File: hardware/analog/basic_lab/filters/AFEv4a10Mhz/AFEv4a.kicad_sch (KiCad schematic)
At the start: 15 parts, among them J1 Connector_Generic_Conn_01x20, J2 Connector_Generic_Conn_01x02, J3 Connector_Generic_Conn_01x02

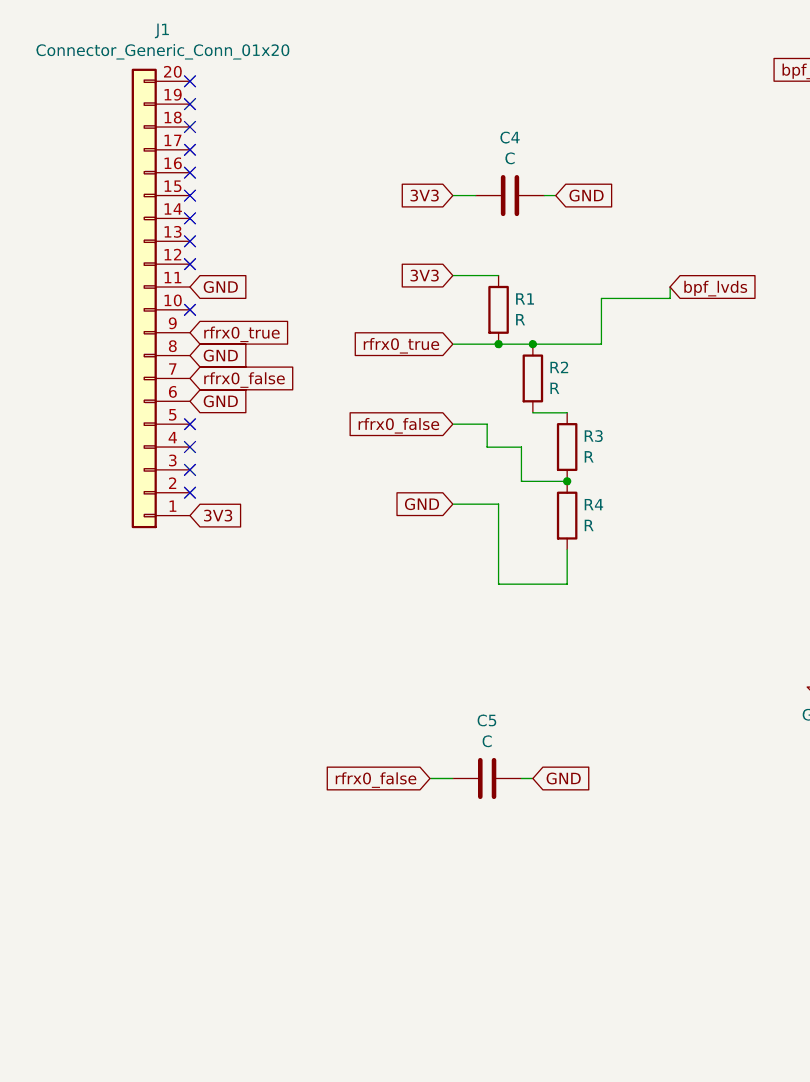
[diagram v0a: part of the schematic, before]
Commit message: started zero DC-offset AFE
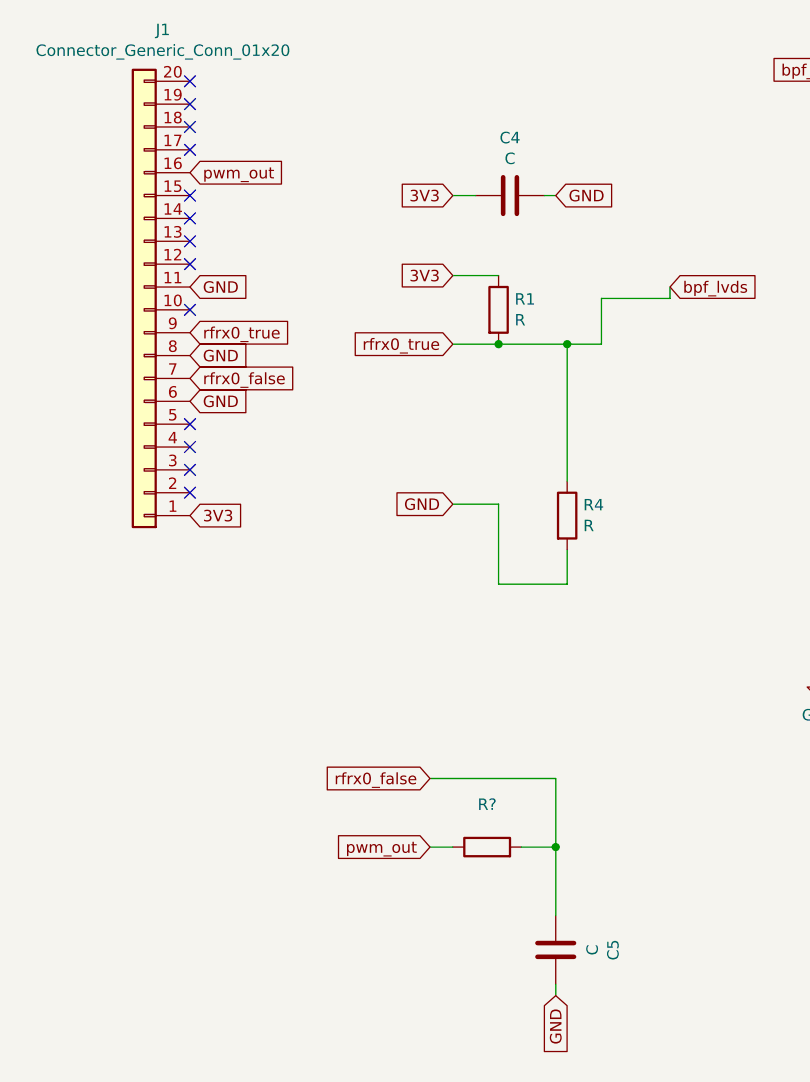
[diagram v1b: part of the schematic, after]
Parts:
- removed R2, R3: R, Resistor_THT:R_Axial_DIN0207_L6.3mm_D2.5mm_P5.08mm_Vertical, symbol Device:R
- added R?: (no value), symbol Device:R
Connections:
- net bpf_lvds: now also R4.1
- net rfrx0_false: now also R?.2; no longer R4.1
- net pwm_out: now reaches J1.16 (Pin_16)
- net pwm_out: now also R?.1
- no-connect marks 14 -> 13
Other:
- moved on the sheet: C5
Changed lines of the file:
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@@
 (kicad_sch (version 20211123) (generator eeschema)
   (paper "A4")
+  (junction (at 86.36 142.24) (diameter 0) (color 0 0 0 0)
+  )
+  (junction (at 87.63 86.36) (diameter 0) (color 0 0 0 0)
+  )
   (junction (at 175.26 80.01) (diameter 0) (color 0 0 0 0)
   )
   (junction (at 165.1 80.01) (diameter 0) (color 0 0 0 0)
-  )
-  (junction (at 83.82 86.36) (diameter 0) (color 0 0 0 0)
-  )
-  (junction (at 87.63 101.6) (diameter 0) (color 0 0 0 0)
   )
   (junction (at 80.01 86.36) (diameter 0) (color 0 0 0 0)
@@
   (no_connect (at 45.72 77.47))
   (no_connect (at 45.72 72.39))
-  (no_connect (at 45.72 67.31))
   (no_connect (at 45.72 97.79))
   (no_connect (at 45.72 82.55))
@@
     (stroke (width 0) (type default) (color 0 0 0 0))
   )
+  (wire (pts (xy 87.63 86.36) (xy 87.63 101.6))
+    (stroke (width 0) (type default) (color 0 0 0 0))
+  )
   (wire (pts (xy 165.1 92.71) (xy 165.1 101.6))
     (stroke (width 0) (type default) (color 0 0 0 0))
@@
     (stroke (width 0) (type default) (color 0 0 0 0))
   )
+  (wire (pts (xy 82.55 142.24) (xy 86.36 142.24))
+    (stroke (width 0) (type default) (color 0 0 0 0))
+  )
   (wire (pts (xy 165.1 80.01) (xy 175.26 80.01))
     (stroke (width 0) (type default) (color 0 0 0 0))
@@
     (stroke (width 0) (type default) (color 0 0 0 0))
   )
-  (wire (pts (xy 78.74 97.79) (xy 78.74 95.25))
-    (stroke (width 0) (type default) (color 0 0 0 0))
-  )
-  (wire (pts (xy 72.39 134.62) (xy 74.93 134.62))
+  (wire (pts (xy 72.39 134.62) (xy 86.36 134.62))
     (stroke (width 0) (type default) (color 0 0 0 0))
   )
@@
     (stroke (width 0) (type default) (color 0 0 0 0))
   )
-  (wire (pts (xy 83.82 86.36) (xy 80.01 86.36))
-    (stroke (width 0) (type default) (color 0 0 0 0))
-  )
-  (wire (pts (xy 82.55 97.79) (xy 78.74 97.79))
-    (stroke (width 0) (type default) (color 0 0 0 0))
-  )
-  (wire (pts (xy 83.82 93.98) (xy 87.63 93.98))
+  (wire (pts (xy 80.01 86.36) (xy 87.63 86.36))
     (stroke (width 0) (type default) (color 0 0 0 0))
   )
@@
     (stroke (width 0) (type default) (color 0 0 0 0))
   )
-  (wire (pts (xy 82.55 134.62) (xy 83.82 134.62))
+  (wire (pts (xy 86.36 157.48) (xy 86.36 158.75))
     (stroke (width 0) (type default) (color 0 0 0 0))
   )
@@
     (stroke (width 0) (type default) (color 0 0 0 0))
   )
+  (wire (pts (xy 86.36 142.24) (xy 86.36 149.86))
+    (stroke (width 0) (type default) (color 0 0 0 0))
+  )
   (wire (pts (xy 175.26 80.01) (xy 184.15 80.01))
     (stroke (width 0) (type default) (color 0 0 0 0))
   )
-  (wire (pts (xy 82.55 101.6) (xy 82.55 97.79))
+  (wire (pts (xy 86.36 134.62) (xy 86.36 142.24))
     (stroke (width 0) (type default) (color 0 0 0 0))
   )
@@
     (stroke (width 0) (type default) (color 0 0 0 0))
   )
-  (wire (pts (xy 78.74 95.25) (xy 74.93 95.25))
-    (stroke (width 0) (type default) (color 0 0 0 0))
-  )
-  (wire (pts (xy 83.82 86.36) (xy 91.44 86.36))
-    (stroke (width 0) (type default) (color 0 0 0 0))
-  )
   (wire (pts (xy 175.26 101.6) (xy 175.26 92.71))
     (stroke (width 0) (type default) (color 0 0 0 0))
@@
     (stroke (width 0) (type default) (color 0 0 0 0))
   )
-  (wire (pts (xy 87.63 101.6) (xy 82.55 101.6))
-    (stroke (width 0) (type default) (color 0 0 0 0))
-  )
   (wire (pts (xy 87.63 113.03) (xy 87.63 109.22))
     (stroke (width 0) (type default) (color 0 0 0 0))
@@
     (stroke (width 0) (type default) (color 0 0 0 0))
   )
+  (wire (pts (xy 87.63 86.36) (xy 91.44 86.36))
+    (stroke (width 0) (type default) (color 0 0 0 0))
+  )
+  (wire (pts (xy 72.39 142.24) (xy 74.93 142.24))
+    (stroke (width 0) (type default) (color 0 0 0 0))
+  )
   (wire (pts (xy 124.46 80.01) (xy 129.54 80.01))
     (stroke (width 0) (type default) (color 0 0 0 0))
@@
     )
   )
+  (global_label "pwm_out" (shape input) (at 45.72 67.31 0) (fields_autoplaced)
+    (effects (font (size 1.27 1.27)) (justify left))
+    (property "Intersheet References" "${INTERSHEET_REFS}" (id 0) (at 56.2085 67.2306 0)
+      (effects (font (size 1.27 1.27)) (justify left) hide)
+    )
+  )
   (global_label "rfrx0_true" (shape input) (at 74.93 86.36 180) (fields_autoplaced)
     (effects (font (size 1.27 1.27)) (justify right))
@@
     )
   )
+  (global_label "pwm_out" (shape input) (at 72.39 142.24 180) (fields_autoplaced)
+    (effects (font (size 1.27 1.27)) (justify right))
+    (property "Intersheet References" "${INTERSHEET_REFS}" (id 0) (at 61.9015 142.3194 0)
+      (effects (font (size 1.27 1.27)) (justify right) hide)
+    )
+  )
   (global_label "GND" (shape input) (at 125.73 111.76 0) (fields_autoplaced)
     (effects (font (size 1.27 1.27)) (justify left))
@@
     )
   )
-  (global_label "GND" (shape input) (at 83.82 134.62 0) (fields_autoplaced)
-    (effects (font (size 1.27 1.27)) (justify left))
-    (property "Intersheet References" "${INTERSHEET_REFS}" (id 0) (at 0 0 0)
+  (global_label "GND" (shape input) (at 86.36 158.75 270) (fields_autoplaced)
+    (effects (font (size 1.27 1.27)) (justify right))
+    (property "Intersheet References" "${INTERSHEET_REFS}" (id 0) (at 220.98 74.93 0)
       (effects (font (size 1.27 1.27)) hide)
     )
@@
   )
   (global_label "GND" (shape input) (at 161.29 134.62 180) (fields_autoplaced)
-    (effects (font (size 1.27 1.27)) (justify right))
-    (property "Intersheet References" "${INTERSHEET_REFS}" (id 0) (at 0 0 0)
-      (effects (font (size 1.27 1.27)) hide)
-    )
-  )
-  (global_label "rfrx0_false" (shape input) (at 74.93 95.25 180) (fields_autoplaced)
     (effects (font (size 1.27 1.27)) (justify right))
     (property "Intersheet References" "${INTERSHEET_REFS}" (id 0) (at 0 0 0)
@@
     (pin "2")
   )
-  (symbol (lib_id "Device:R") (at 83.82 90.17 0) (unit 1)
-    (in_bom yes) (on_board yes)
-    (property "Reference" "R2" (id 0) (at 85.598 89.0016 0)
-      (effects (font (size 1.27 1.27)) (justify left))
-    )
-    (property "Value" "R" (id 1) (at 85.598 91.313 0)
-      (effects (font (size 1.27 1.27)) (justify left))
-    )
-    (property "Footprint" "Resistor_THT:R_Axial_DIN0207_L6.3mm_D2.5mm_P5.08mm_Vertical" (id 2) (at 82.042 90.17 90)
-      (effects (font (size 1.27 1.27)) hide)
-    )
-    (property "Datasheet" "~" (id 3) (at 83.82 90.17 0)
-      (effects (font (size 1.27 1.27)) hide)
-    )
-    (pin "1")
-    (pin "2")
-  )
-  (symbol (lib_id "Device:R") (at 87.63 97.79 0) (unit 1)
-    (in_bom yes) (on_board yes)
-    (property "Reference" "R3" (id 0) (at 89.408 96.6216 0)
-      (effects (font (size 1.27 1.27)) (justify left))
-    )
-    (property "Value" "R" (id 1) (at 89.408 98.933 0)
-      (effects (font (size 1.27 1.27)) (justify left))
-    )
-    (property "Footprint" "Resistor_THT:R_Axial_DIN0207_L6.3mm_D2.5mm_P5.08mm_Vertical" (id 2) (at 85.852 97.79 90)
-      (effects (font (size 1.27 1.27)) hide)
-    )
-    (property "Datasheet" "~" (id 3) (at 87.63 97.79 0)
-      (effects (font (size 1.27 1.27)) hide)
-    )
-    (pin "1")
-    (pin "2")
-  )
   (symbol (lib_id "Device:R") (at 87.63 105.41 0) (unit 1)
     (in_bom yes) (on_board yes)
@@
     (pin "2")
   )
-  (symbol (lib_id "Device:C") (at 78.74 134.62 270) (unit 1)
-    (in_bom yes) (on_board yes)
-    (property "Reference" "C5" (id 0) (at 78.74 128.2192 90))
-    (property "Value" "C" (id 1) (at 78.74 130.5306 90))
-    (property "Footprint" "Capacitor_THT:C_Axial_L5.1mm_D3.1mm_P15.00mm_Horizontal" (id 2) (at 74.93 135.5852 0)
-      (effects (font (size 1.27 1.27)) hide)
-    )
-    (property "Datasheet" "~" (id 3) (at 78.74 134.62 0)
+  (symbol (lib_id "Device:C") (at 86.36 153.67 180) (unit 1)
+    (in_bom yes) (on_board yes)
+    (property "Reference" "C5" (id 0) (at 92.7608 153.67 90))
+    (property "Value" "C" (id 1) (at 90.4494 153.67 90))
+    (property "Footprint" "Capacitor_THT:C_Axial_L5.1mm_D3.1mm_P15.00mm_Horizontal" (id 2) (at 85.3948 149.86 0)
+      (effects (font (size 1.27 1.27)) hide)
+    )
+    (property "Datasheet" "~" (id 3) (at 86.36 153.67 0)
+      (effects (font (size 1.27 1.27)) hide)
+    )
+    (pin "1")
+    (pin "2")
+  )
+  (symbol (lib_id "Device:R") (at 78.74 142.24 90) (unit 1)
+    (in_bom yes) (on_board yes) (fields_autoplaced)
+    (property "Reference" "R?" (id 0) (at 78.74 137.5242 90))
+    (property "Value" "" (id 1) (at 78.74 140.0611 90))
+    (property "Footprint" "" (id 2) (at 78.74 144.018 90)
+      (effects (font (size 1.27 1.27)) hide)
+    )
+    (property "Datasheet" "~" (id 3) (at 78.74 142.24 0)
       (effects (font (size 1.27 1.27)) hide)
     )
@@
       (reference "R1") (unit 1) (value "R") (footprint "Resistor_THT:R_Axial_DIN0207_L6.3mm_D2.5mm_P5.08mm_Vertical")
     )
-    (path "/00000000-0000-0000-0000-000061f84d92"
-      (reference "R2") (unit 1) (value "R") (footprint "Resistor_THT:R_Axial_DIN0207_L6.3mm_D2.5mm_P5.08mm_Vertical")
-    )
-    (path "/00000000-0000-0000-0000-000061f84fe9"
-      (reference "R3") (unit 1) (value "R") (footprint "Resistor_THT:R_Axial_DIN0207_L6.3mm_D2.5mm_P5.08mm_Vertical")
-    )
     (path "/00000000-0000-0000-0000-000061f8539c"
       (reference "R4") (unit 1) (value "R") (footprint "Resistor_THT:R_Axial_DIN0207_L6.3mm_D2.5mm_P5.08mm_Vertical")
     )
-  )
+    (path "/08d5e7dc-4237-4aba-b163-40b464880915"
+      (reference "R?") (unit 1) (value "R") (footprint "")
+    )
+  )
